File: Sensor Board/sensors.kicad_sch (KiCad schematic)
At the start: 11 parts, among them J1 Conn_Sensors, U1 LSM6DSM, U2 ADC081C021CIMM

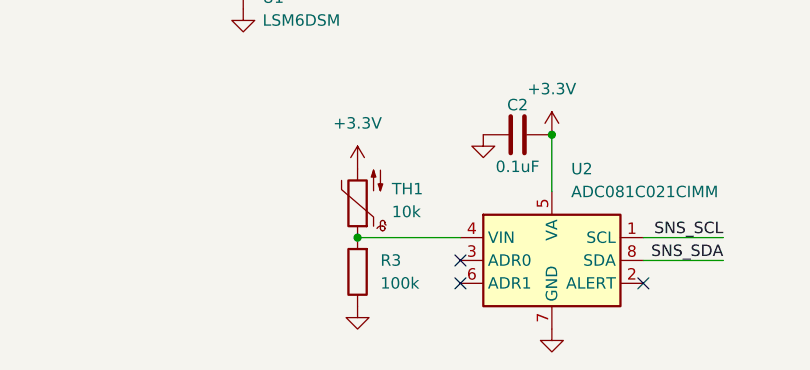
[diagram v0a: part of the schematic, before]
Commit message: Add part numbers to remaining PCBs, change part numbers on sensor board, redo strain adc layout
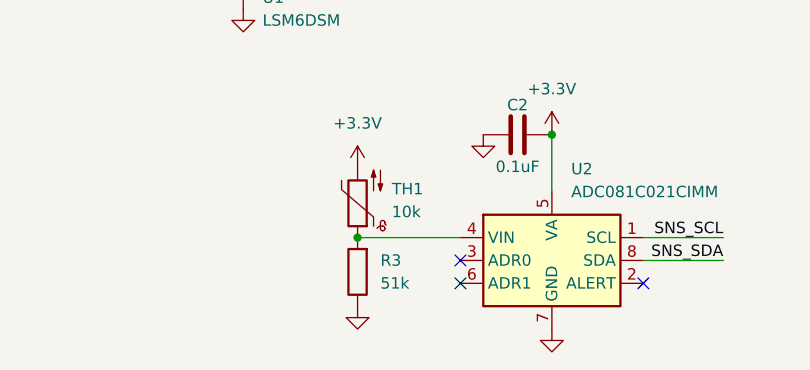
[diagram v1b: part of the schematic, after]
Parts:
- C1: MPN 0402W106M6R3HI -> CL05A106MQ5NUNC
- C2, C3, C4: MPN 0402B104K160HI -> CL05B104KP5NNNC
- R1, R2: MPN RC0402JR-074K7L -> RC0402FR-074K7L
- R3: value 100k -> 51k; MPN RC0402JR-07100KL -> ERJ-2RKF5102X
- TH1: MPN NCU15XH103F6SRC -> RC0402JR-0710KL
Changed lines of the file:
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@@
 			)
 		)
-		(property "MPN" "0402W106M6R3HI"
+		(property "MPN" "CL05A106MQ5NUNC"
 			(at 180.34 76.2 0)
 			(effects
@@
 			)
 		)
-		(property "MPN" "0402B104K160HI"
+		(property "MPN" "CL05B104KP5NNNC"
 			(at 133.35 68.58 0)
 			(effects
@@
 			)
 		)
-		(property "MPN" "RC0402JR-074K7L"
+		(property "MPN" "RC0402FR-074K7L"
 			(at 163.83 93.98 0)
 			(effects
@@
 			)
 		)
-		(property "MPN" "RC0402JR-074K7L"
+		(property "MPN" "RC0402FR-074K7L"
 			(at 163.83 81.28 0)
 			(effects
@@
 			)
 		)
-		(property "MPN" "0402B104K160HI"
+		(property "MPN" "CL05B104KP5NNNC"
 			(at 146.05 116.84 0)
 			(effects
@@
 			)
 		)
-		(property "Value" "100k"
+		(property "Value" "51k"
 			(at 130.81 133.3499 0)
 			(effects
@@
 			)
 		)
-		(property "MPN" "RC0402JR-07100KL"
+		(property "MPN" "ERJ-2RKF5102X"
 			(at 128.27 132.08 0)
 			(effects
@@
 			)
 		)
-		(property "MPN" "NCU15XH103F6SRC"
+		(property "MPN" "RC0402JR-0710KL"
 			(at 128.27 124.46 0)
 			(effects
@@
 			)
 		)
-		(property "MPN" "0402B104K160HI"
+		(property "MPN" "CL05B104KP5NNNC"
 			(at 128.27 68.58 0)
 			(effects
